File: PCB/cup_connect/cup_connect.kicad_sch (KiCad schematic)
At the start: 8 parts, among them J1 Connect, J2 EXT, U1 LDO-3.3

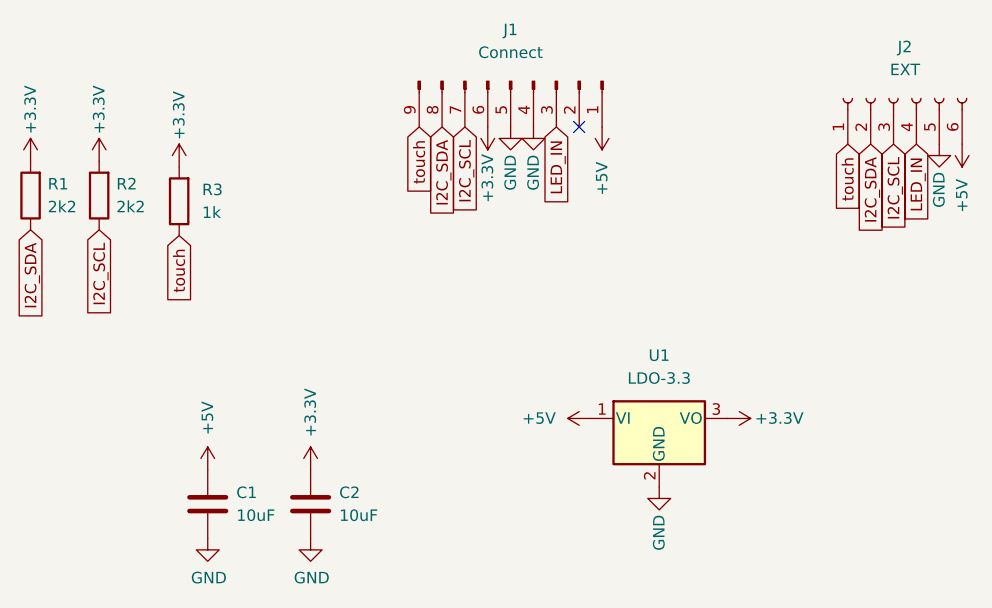
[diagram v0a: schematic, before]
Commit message: fix schematic values
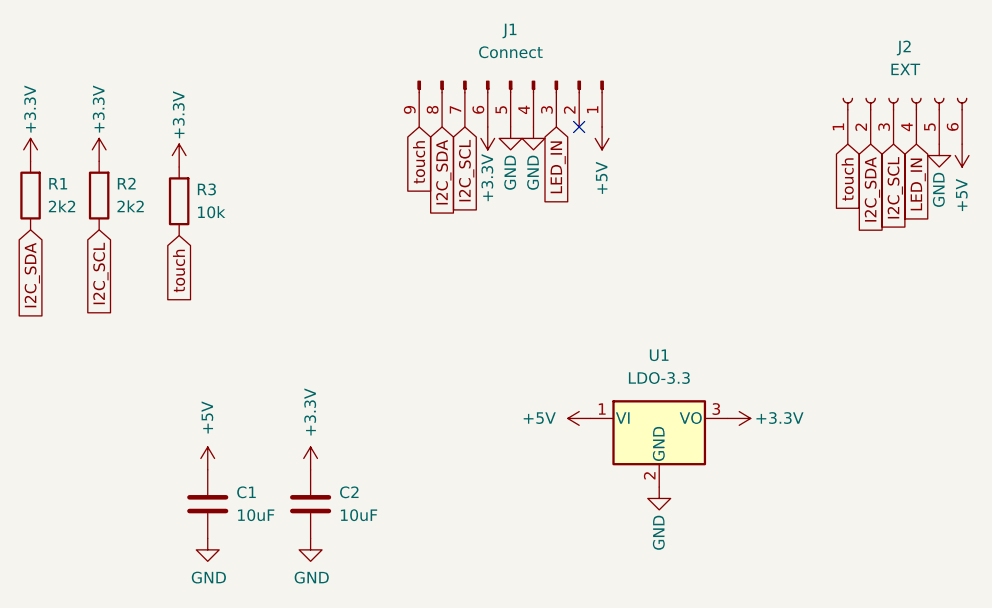
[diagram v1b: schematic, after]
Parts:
- R3: value 1k -> 10k
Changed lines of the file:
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@@
   (symbol (lib_id "Device:R") (at 90.805 79.375 180) (unit 1)
     (in_bom yes) (on_board yes) (fields_autoplaced)
-    (property "Reference" "R3" (id 0) (at 93.345 78.1049 0)
+    (property "Reference" "R3" (id 0) (at 92.71 78.1049 0)
       (effects (font (size 1.27 1.27)) (justify right))
     )
-    (property "Value" "1k" (id 1) (at 93.345 80.6449 0)
+    (property "Value" "10k" (id 1) (at 92.71 80.6449 0)
       (effects (font (size 1.27 1.27)) (justify right))
     )
@@
     )
     (path "/4f89e6d3-b4c0-41b0-a20a-c73dae3dbbf4"
-      (reference "R3") (unit 1) (value "1k") (footprint "Resistor_SMD:R_0603_1608Metric")
+      (reference "R3") (unit 1) (value "10k") (footprint "Resistor_SMD:R_0603_1608Metric")
     )
     (path "/18ccab49-4f0a-4a8f-91d1-fbe0ca5b7445"
